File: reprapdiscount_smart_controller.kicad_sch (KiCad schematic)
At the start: 38 parts, among them Q1 BC817, Q2 BC817, U1 74HC4050, U2 AMS1117-3.3

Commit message: silkscreen: update to match ldo-rrlcd-a007
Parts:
- C4: footprint Capacitor_SMD:C_1206_3216Metric_Pad1.33x1.80mm_HandSolder -> Capacitor_SMD:C_0805_2012Metric_Pad1.18x1.45mm_HandSolder
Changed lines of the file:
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@@
       (effects (font (size 1.27 1.27)) (justify left))
     )
-    (property "Footprint" "Capacitor_SMD:C_1206_3216Metric_Pad1.33x1.80mm_HandSolder" (at 219.4052 124.46 0)
+    (property "Footprint" "Capacitor_SMD:C_0805_2012Metric_Pad1.18x1.45mm_HandSolder" (at 219.4052 124.46 0)
       (effects (font (size 1.27 1.27)) hide)
     )

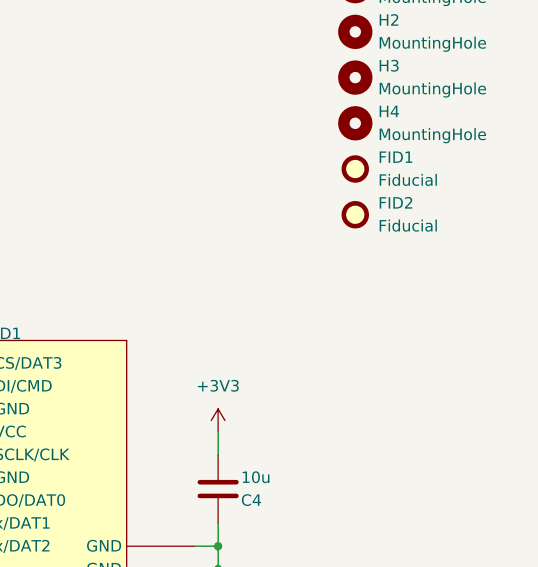
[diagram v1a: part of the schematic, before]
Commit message: feature: add back side fiducials
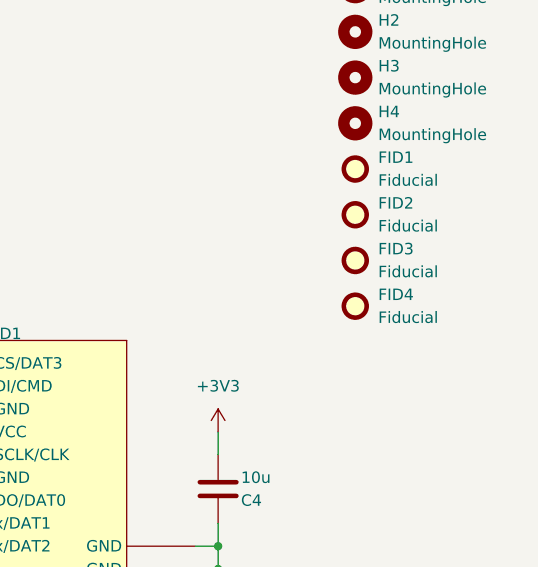
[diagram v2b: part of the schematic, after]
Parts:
- added FID3, FID4: Fiducial, Fiducial:Fiducial_1mm_Mask2mm, symbol Mechanical:Fiducial
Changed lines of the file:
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@@
+    )
+  )
+  (symbol (lib_id "Mechanical:Fiducial") (at 233.68 102.87 0) (unit 1)
+    (in_bom yes) (on_board yes) (dnp no) (fields_autoplaced)
+    (property "Reference" "FID3" (at 236.22 101.6 0)
+      (effects (font (size 1.27 1.27)) (justify left))
+    )
+    (property "Value" "Fiducial" (at 236.22 104.14 0)
+      (effects (font (size 1.27 1.27)) (justify left))
+    )
+    (property "Footprint" "Fiducial:Fiducial_1mm_Mask2mm" (at 233.68 102.87 0)
+      (effects (font (size 1.27 1.27)) hide)
+    )
+    (property "Datasheet" "~" (at 233.68 102.87 0)
+      (effects (font (size 1.27 1.27)) hide)
+    )
+    (instances
+      (project "reprapdiscount_smart_controller"
+        (path "/c20eb3f6-d157-43e2-84ab-82664a430dd1"
+          (reference "FID3") (unit 1)
+        )
+      )
     )
   )
@@
         )
       )
+    )
+  )
+  (symbol (lib_id "Mechanical:Fiducial") (at 233.68 107.95 0) (unit 1)
+    (in_bom yes) (on_board yes) (dnp no) (fields_autoplaced)
+    (property "Reference" "FID4" (at 236.22 106.68 0)
+      (effects (font (size 1.27 1.27)) (justify left))
+    )
+    (property "Value" "Fiducial" (at 236.22 109.22 0)
+      (effects (font (size 1.27 1.27)) (justify left))
+    )
+    (property "Footprint" "Fiducial:Fiducial_1mm_Mask2mm" (at 233.68 107.95 0)
+      (effects (font (size 1.27 1.27)) hide)
+    )
+    (property "Datasheet" "~" (at 233.68 107.95 0)
+      (effects (font (size 1.27 1.27)) hide)
+    )
+    (instances
+      (project "reprapdiscount_smart_controller"
+        (path "/c20eb3f6-d157-43e2-84ab-82664a430dd1"
+          (reference "FID4") (unit 1)
+        )
+      )

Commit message: feature: add revision info to builds
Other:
- title: (none) -> RepRapDiscount.com Smart Controller
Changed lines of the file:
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@@
 (kicad_sch (version 20230121) (generator eeschema)
   (paper "A")
+  (title_block
+    (title "RepRapDiscount.com Smart Controller")
+    (date "${DATE}")
+    (rev "${TAG} (${REVISION})")
+  )
   (junction (at 128.27 43.18) (diameter 0) (color 0 0 0 0)
   )

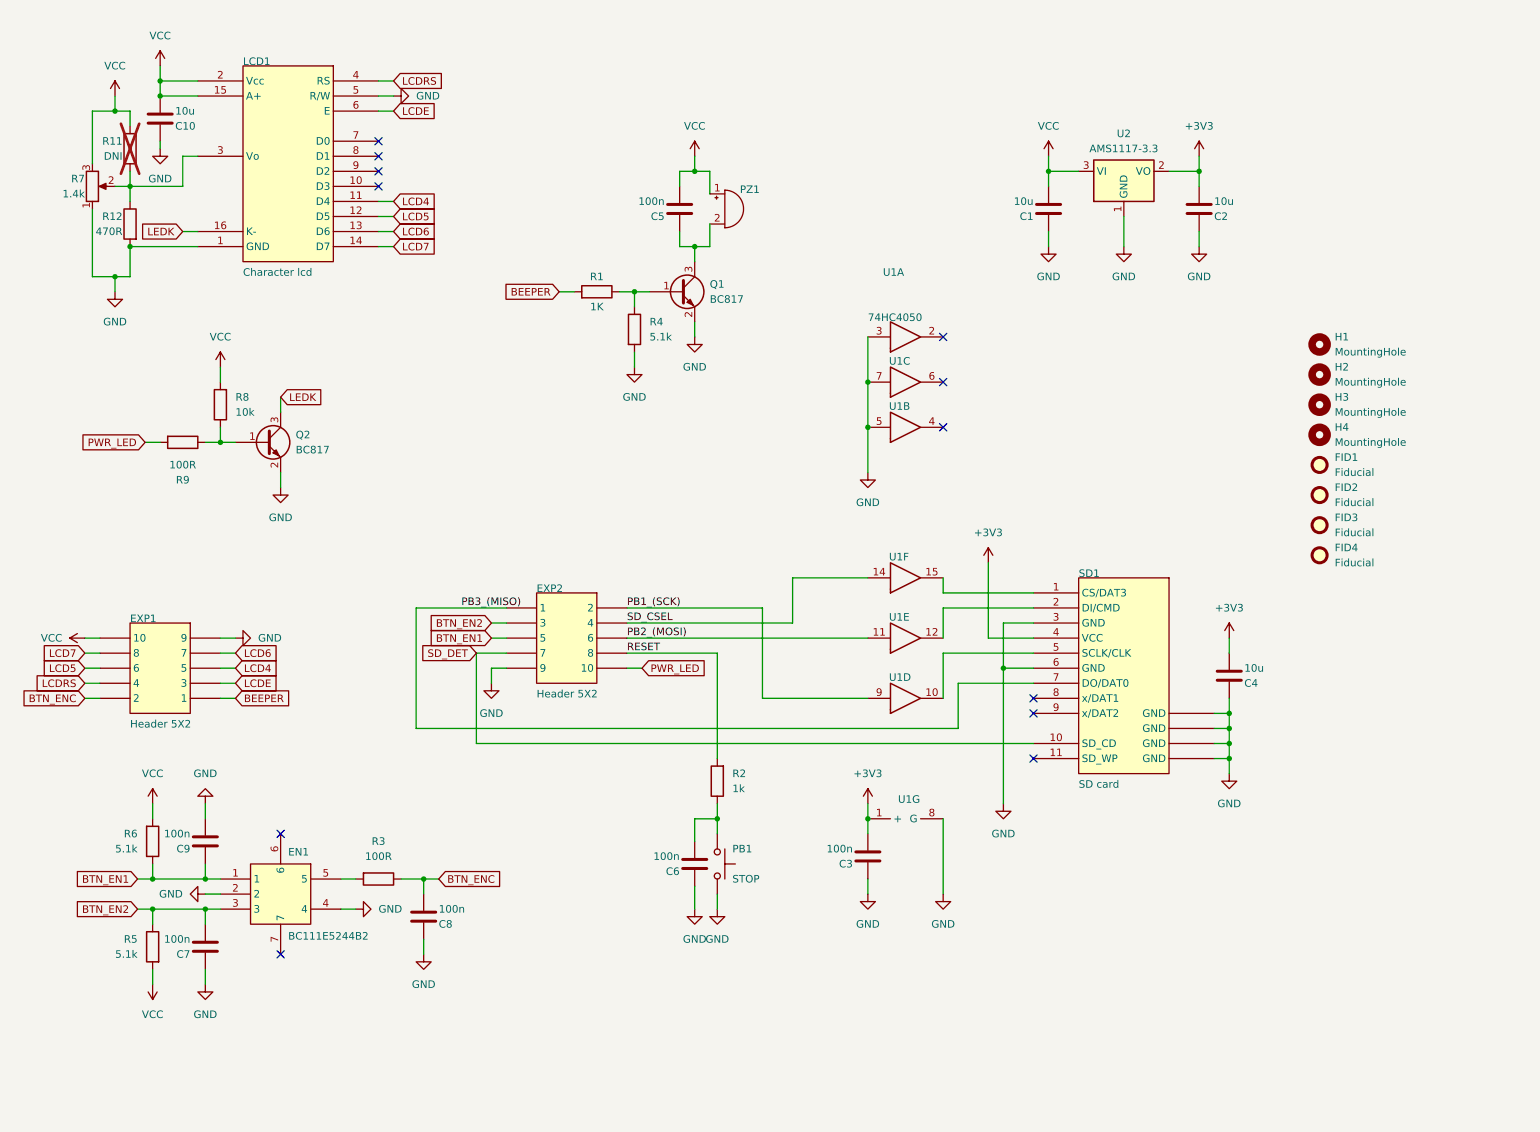
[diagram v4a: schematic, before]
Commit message: feature: redesign for usb host functionality
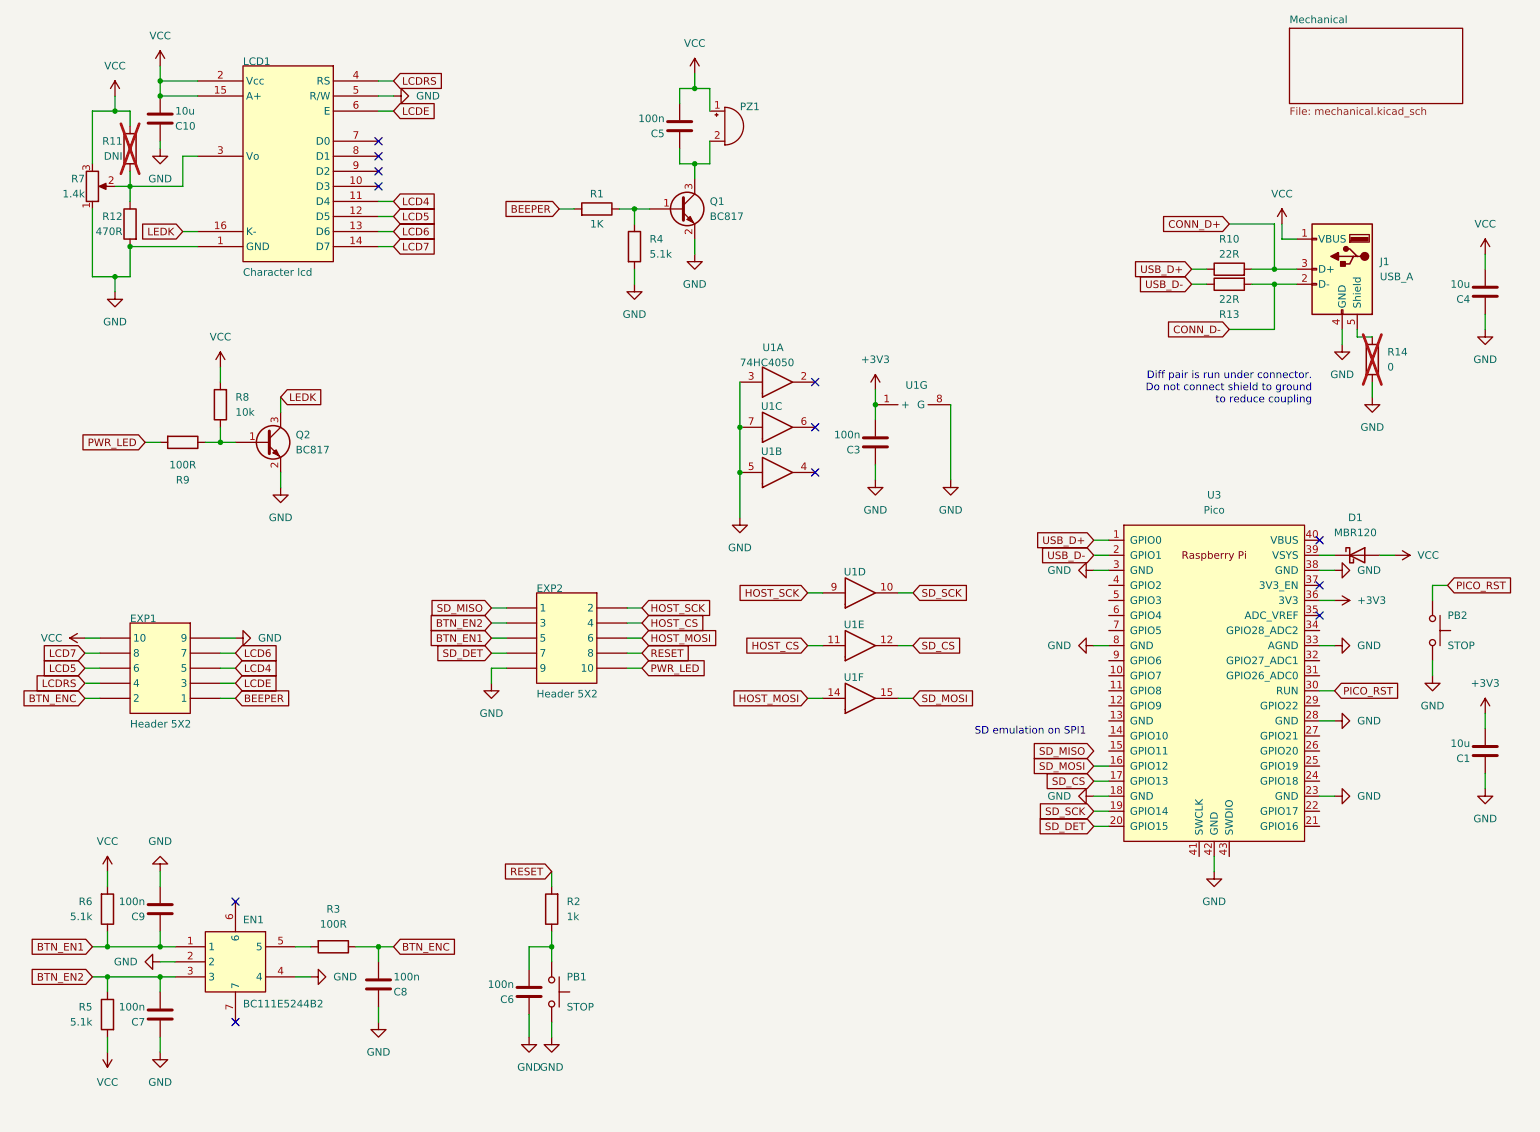
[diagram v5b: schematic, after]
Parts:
- removed C2: 10u, Capacitor_SMD:C_0805_2012Metric_Pad1.18x1.45mm_HandSolder, symbol Device:C
- removed FID1, FID2, FID3, FID4: Fiducial, Fiducial:Fiducial_1mm_Mask2mm, symbol Mechanical:Fiducial
- removed H1, H2, H3, H4: MountingHole, reprapdiscount_smart_controller:MountingHole_3mm, symbol Mechanical:MountingHole
- removed SD1: SD card, reprapdiscount_smart_controller:SD_card socket, symbol reprapdiscount_smart_controller-altium-import:root_0_SD card
- removed U2: AMS1117-3.3, Package_TO_SOT_SMD:SOT-223-3_TabPin2, symbol Regulator_Linear:AMS1117-3.3
- added D1: MBR120, Diode_SMD:D_SOD-123, symbol Device:D_Schottky
- added J1: USB_A, Gigahawk:USB_A_Stewart_SS-52100-001_Horizontal, symbol Connector:USB_A
- added PB2: STOP, Button_Switch_THT:SW_PUSH_6mm_H7.3mm, symbol Switch:SW_Push
- added R10, R13: 22R, Resistor_SMD:R_0805_2012Metric_Pad1.20x1.40mm_HandSolder, symbol Device:R
- added R14: 0, Resistor_SMD:R_0805_2012Metric_Pad1.20x1.40mm_HandSolder, symbol Device:R
- added U3: Pico, Gigahawk:RPi_Pico_SMD_NO_SILK, symbol gigahawk:Pico
- C4: ALTIUM_VALUE 1uF -> 100nF
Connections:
- net +3V3: now also C1.2, U3.36 (3V3); no longer C4.2
- net GND: now also J1.4 (GND), PB2.2, R14.2, U3.18 (GND), U3.23 (GND), U3.28 (GND), U3.3 (GND), U3.33 (AGND), U3.38 (GND), U3.42 (GND), U3.8 (GND)
- net SD_DET: now also U3.20 (GPIO15)
- net VCC: now also C4.2, D1.2 (A), J1.1 (VBUS); no longer C1.2
- net SD_SCK: now reaches U1.10
- net SD_SCK: now also U3.19 (GPIO14)
- net SD_CS: now reaches U1.12
- net SD_CS: now also U3.17 (GPIO13)
- net SD_MOSI: now reaches U1.15
- net SD_MOSI: now also U3.16 (GPIO12)
- net PB1_(SCK) renamed HOST_SCK
- net PB2_(MOSI) renamed HOST_CS
- net HOST_CS: now also EXP2.4; no longer EXP2.6
- net PB3_(MISO) renamed SD_MISO
- net SD_CSEL renamed HOST_MOSI
- net HOST_MOSI: now also EXP2.6; no longer EXP2.4
- new net: D1.1 (K), U3.39 (VSYS)
- new net: J1.5 (Shield), R14.1
- new net CONN_D+: J1.3 (D+), R10.2
- new net CONN_D-: J1.2 (D-), R13.2
- new net PICO_RST: PB2.1, U3.30 (RUN)
- new net USB_D+: R10.1, U3.1 (GPIO0)
- new net USB_D-: R13.1, U3.2 (GPIO1)
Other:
- added sheet Mechanical (mechanical.kicad_sch)
- note added: "Diff pair is run under connector. Do not connect shield to ground to reduce coupling"
- note added: "SD emulation on SPI1"
- moved on the sheet: C3, C5, C6, C7, C8, C9, EN1, PB1, PZ1, Q1, R1, R2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

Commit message: layout: minor fixes and adjustments
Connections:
- net SD_MISO: now also U3.15 (GPIO11)
- no-connect marks 12 -> 32
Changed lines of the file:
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@@
   (no_connect (at 148.59 86.36))
   (no_connect (at 50.8 186.69))
+  (no_connect (at 233.68 128.27))
   (no_connect (at 74.93 45.72))
+  (no_connect (at 233.68 153.67))
+  (no_connect (at 198.12 120.65))
+  (no_connect (at 233.68 143.51))
+  (no_connect (at 233.68 140.97))
   (no_connect (at 233.68 118.11))
   (no_connect (at 74.93 43.18))
+  (no_connect (at 198.12 125.73))
+  (no_connect (at 198.12 130.81))
+  (no_connect (at 198.12 118.11))
   (no_connect (at 148.59 78.74))
   (no_connect (at 148.59 93.98))
+  (no_connect (at 233.68 133.35))
+  (no_connect (at 233.68 125.73))
+  (no_connect (at 198.12 133.35))
+  (no_connect (at 198.12 115.57))
   (no_connect (at 233.68 113.03))
+  (no_connect (at 233.68 120.65))
   (no_connect (at 74.93 38.1))
+  (no_connect (at 198.12 138.43))
+  (no_connect (at 233.68 146.05))
   (no_connect (at 74.93 40.64))
+  (no_connect (at 233.68 151.13))
+  (no_connect (at 198.12 113.03))
   (no_connect (at 50.8 166.37))
   (no_connect (at 233.68 105.41))
+  (no_connect (at 233.68 138.43))
+  (no_connect (at 198.12 135.89))
+  (no_connect (at 198.12 128.27))
   (wire (pts (xy 38.1 173.99) (xy 40.64 173.99))
     (stroke (width 0) (type default))
@@
     (stroke (width 0) (type default))
   )
+  (wire (pts (xy 195.58 140.97) (xy 198.12 140.97))
+    (stroke (width 0) (type default))
+  )
